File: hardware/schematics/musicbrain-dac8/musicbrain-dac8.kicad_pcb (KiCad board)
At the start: 2 copper layers, 50 x 80 mm, 26 parts, among them J1 BUS, J2 CV OUT, U1 AD5754BREZ, U2 AD5754BREZ, U3 ADR421

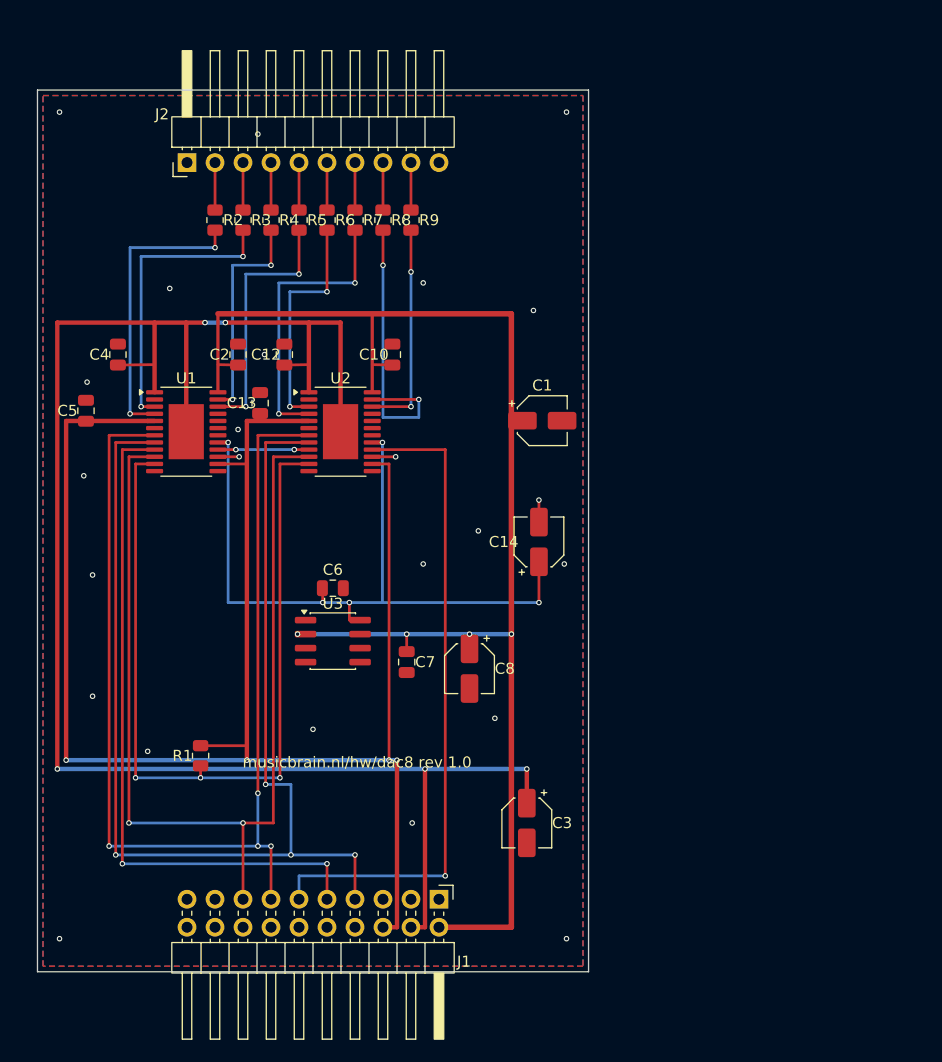
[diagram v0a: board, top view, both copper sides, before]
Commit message: dac8 gen 2: 80x45, slot 2x12, freerouting + DGND-redding
- kaart 50x80 -> 80x45; J1 2x10 -> 2x12 via bus.j1_map; J2 gecentreerd
- DACs onder hun CV-kolommen (U1 -> CV1-4, U2 -> CV5-8); handroutes
  vervangen door freerouting-SES
- DGND-redding (gen-1-les terug): pin 15 zit klem tussen de 0.65-entries;
  vast spoor + via voor freerouting uit
- C5/C13 GND-pad naar de open zuidcorridor (rot 270)
- prep_dsn: keepout-optie toegevoegd maar UIT - freerouting v2.1 meldt
  0 incompleet terwijl netten breken zodra er keepouts in de DSN staan
- ERC 0, netcheck OK, DRC 0/0

Co-Authored-By: Claude Fable 5 <noreply@anthropic.com>
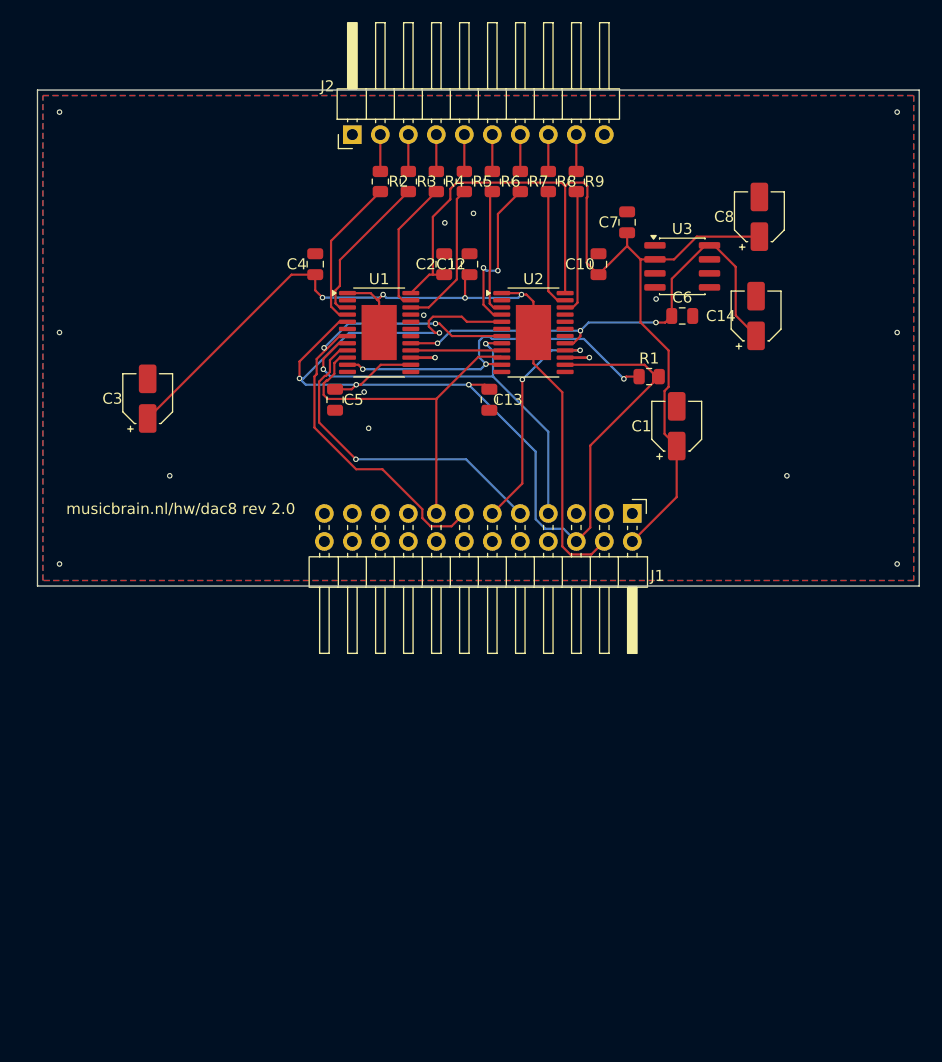
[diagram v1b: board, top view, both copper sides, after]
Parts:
- J1: footprint Connector_PinHeader_2.54mm:PinHeader_2x10_P2.54mm_Horizontal -> Connector_PinHeader_2.54mm:PinHeader_2x12_P2.54mm_Horizontal
- R1: renamed from R9; value 100R -> 10k
- R2: renamed from U1; value AD5754BREZ -> 100R; footprint Package_SO:HTSSOP-24-1EP_4.4x7.8mm_P0.65mm_EP3.2x5mm -> Resistor_SMD:R_0805_2012Metric
- R3: renamed from U2; value AD5754BREZ -> 100R; footprint Package_SO:HTSSOP-24-1EP_4.4x7.8mm_P0.65mm_EP3.2x5mm -> Resistor_SMD:R_0805_2012Metric
- R4: renamed from U3; value ADR421 -> 100R; footprint Package_SO:SOIC-8_3.9x4.9mm_P1.27mm -> Resistor_SMD:R_0805_2012Metric
- R5: renamed from R1; value 10k -> 100R
- U1: renamed from R6; value 100R -> AD5754BREZ; footprint Resistor_SMD:R_0805_2012Metric -> Package_SO:HTSSOP-24-1EP_4.4x7.8mm_P0.65mm_EP3.2x5mm
- U2: renamed from R7; value 100R -> AD5754BREZ; footprint Resistor_SMD:R_0805_2012Metric -> Package_SO:HTSSOP-24-1EP_4.4x7.8mm_P0.65mm_EP3.2x5mm
- U3: renamed from R8; value 100R -> ADR421; footprint Resistor_SMD:R_0805_2012Metric -> Package_SO:SOIC-8_3.9x4.9mm_P1.27mm
- moved R5 57.3 mm to (138.7, 108.3), turned to 270 degrees
- moved C3 51.6 mm to (110.0, 128.0), turned to 90 degrees
- moved C8 48.7 mm to (165.5, 111.5), turned to 90 degrees
- moved C7 44.6 mm to (153.5, 112.0), turned to 90 degrees
- moved R4 42.7 mm to (136.2, 108.3), turned to 270 degrees
- moved C6 40.2 mm to (158.5, 120.5)
- moved J1 39.1 mm to (154.0, 138.4)
- moved R2 28.7 mm to (131.1, 108.3), turned to 270 degrees
- moved C14 28.4 mm to (165.2, 120.5)
- moved U3 27.5 mm to (158.5, 116.0), turned to 0 degrees
- moved R1 25.9 mm to (155.5, 126.0), turned to 0 degrees
- moved R6 25.4 mm to (141.3, 108.3)
- moved R7 25.4 mm to (143.8, 108.3)
- moved R8 25.4 mm to (146.3, 108.3)
- moved R9 25.4 mm to (148.9, 108.3)
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- renumbered R2 to R6, R3 to R7, R4 to R8, R5 to R9
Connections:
- J1 pad 20: (no net) -> GND
- R1 pad 1: /CV8 -> /CLR
- R1 pad 2: /VD2 -> +3V3
- R2 pad 1: -12V -> /CV1
- R2 pad 2: (no net) -> /VB1
- R3 pad 1: -12V -> /CV2
- R3 pad 2: (no net) -> /VA1
- R4 pad 1: (no net) -> /CV3
- R4 pad 2: +12V -> /VC1
- R5 pad 1: /CLR -> /CV4
- R5 pad 2: +3V3 -> /VD1
- R6 pad 1: /CV1 -> /CV5
- R6 pad 2: /VB1 -> /VA2
- R7 pad 1: /CV2 -> /CV6
- R7 pad 2: /VA1 -> /VB2
- R8 pad 1: /CV3 -> /CV7
- R8 pad 2: /VC1 -> /VC2
- R9 pad 1: /CV4 -> /CV8
- R9 pad 2: /VD1 -> /VD2
- U1 pad 1: /CV5 -> -12V
- U1 pad 2: /VA2 -> (no net)
- U2 pad 1: /CV6 -> -12V
- U2 pad 2: /VB2 -> (no net)
- U3 pad 1: /CV7 -> (no net)
- U3 pad 2: /VC2 -> +12V
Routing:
- net -12V: track 160.7 -> 81.5 mm, vias 5 -> 4
- net /SCLK: track 110.3 -> 38.8 mm, vias 4 -> 2
- net /LDAC: track 92.0 -> 33.1 mm, vias 2 -> 0
- net /CS: track 102.8 -> 46.0 mm, vias 4 -> 2
- net +3V3: track 157.6 -> 102.1 mm
- net /CLR: track 75.5 -> 33.1 mm
- net +12V: track 130.8 -> 90.6 mm, vias 4 -> 0
- net /MISO: track 60.7 -> 21.0 mm, vias 1 -> 2
- net /MOSI: track 62.3 -> 29.8 mm, vias 2 -> 1
- net /VREF: track 66.7 -> 45.1 mm, vias 5 -> 3
- net /VC2: track 26.1 -> 10.9 mm, vias 2 -> 0
- net /VB1: track 26.6 -> 14.1 mm, vias 2 -> 0
- net /VA1: track 26.5 -> 14.1 mm, vias 2 -> 0
- net /VB2: track 26.3 -> 14.8 mm
- net /VD1: track 23.4 -> 13.5 mm, vias 2 -> 0
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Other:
- board size 50 x 80 mm -> 80 x 45 mm
- board text added: "musicbrain.nl/hw/dac8 rev 2.0"
- board text removed: "musicbrain.nl/hw/dac8 rev 1.0"

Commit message: afslank-ronde: potriser 40, gatein8 50, gate8 55, dac8 60, adc8 65 (x45)
80 mm was een maximum, geen eis (observatie Mark): J1/J2 blijven op de
hartlijn, de rand schuift naar binnen. Silk verticaal in de westrand
(horizontaal paste niet meer); hoekvia's geparametriseerd op BX0/BX1;
zwervers mee (gate8 C1, dac8 C3, adc8 JP1). Alle vijf opnieuw geroute
(verse SES) en op ERC 0 + netcheck OK + DRC 0/0.

Co-Authored-By: Claude Fable 5 <noreply@anthropic.com>
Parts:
- moved C3 5.00 mm to (115.0, 128.0)
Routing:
- net -12V: track 81.5 -> 99.7 mm
- net /VREF: track 45.1 -> 53.9 mm
- net /LDAC: track 33.1 -> 41.0 mm, vias 0 -> 1
- net /VA2: track 11.5 -> 17.5 mm, vias 0 -> 2
- net +12V: track 90.6 -> 87.3 mm
- net /MISO: track 21.0 -> 22.5 mm, vias 2 -> 1
- net /VB2: track 14.8 -> 13.6 mm, vias 2 -> 0
- net /SCLK: track 38.8 -> 37.9 mm, vias 2 -> 3
- net +3V3: track 102.1 -> 101.4 mm, vias 4 -> 5
- net /CLR: track 33.1 -> 32.5 mm, vias 3 -> 0
- net /MOSI: track 29.8 -> 30.2 mm, vias 1 -> 0
- net GND: vias 16 -> 15
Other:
- board size 80 x 45 mm -> 60 x 45 mm
